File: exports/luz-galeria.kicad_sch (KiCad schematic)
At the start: 40 parts

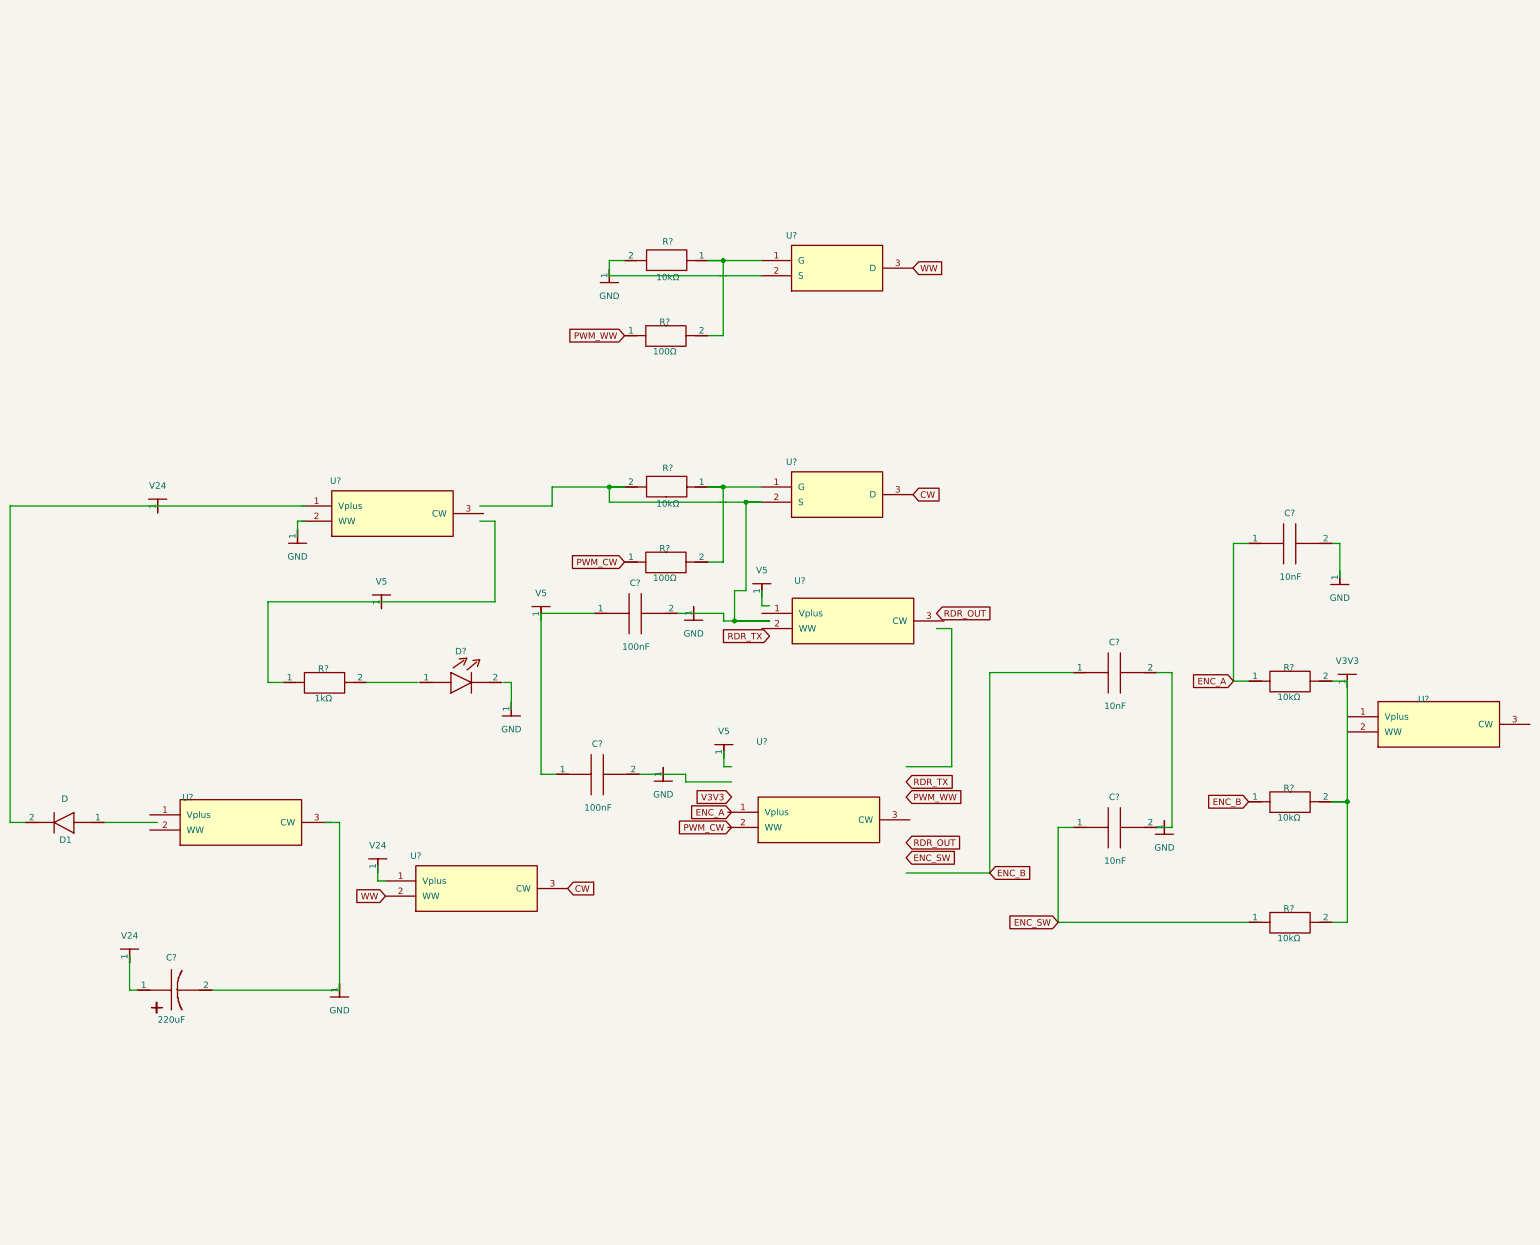
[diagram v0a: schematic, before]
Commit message: Fix EC11 encoder left unconnected by empty KiCad footprint
The kicad: footprint for the Alps EC11E resolved to zero pads in this
tscircuit version, so all seven encoder traces were silently dropped and
the encoder had no electrical connection in the netlist.

Replace it with a self-contained Ec11Footprint (geometry transcribed from
the official KiCad library: C/A/B/S1/S2 signal pads + two 2.5mm mounting
posts) with named ports, and wire MP1/MP2 to GND. Also add React keys to
the ESP32 footprint hole list to clear the render warning.

https://claude.ai/code/session_01ShC9W1aj1k3gaTpsgCGkmU
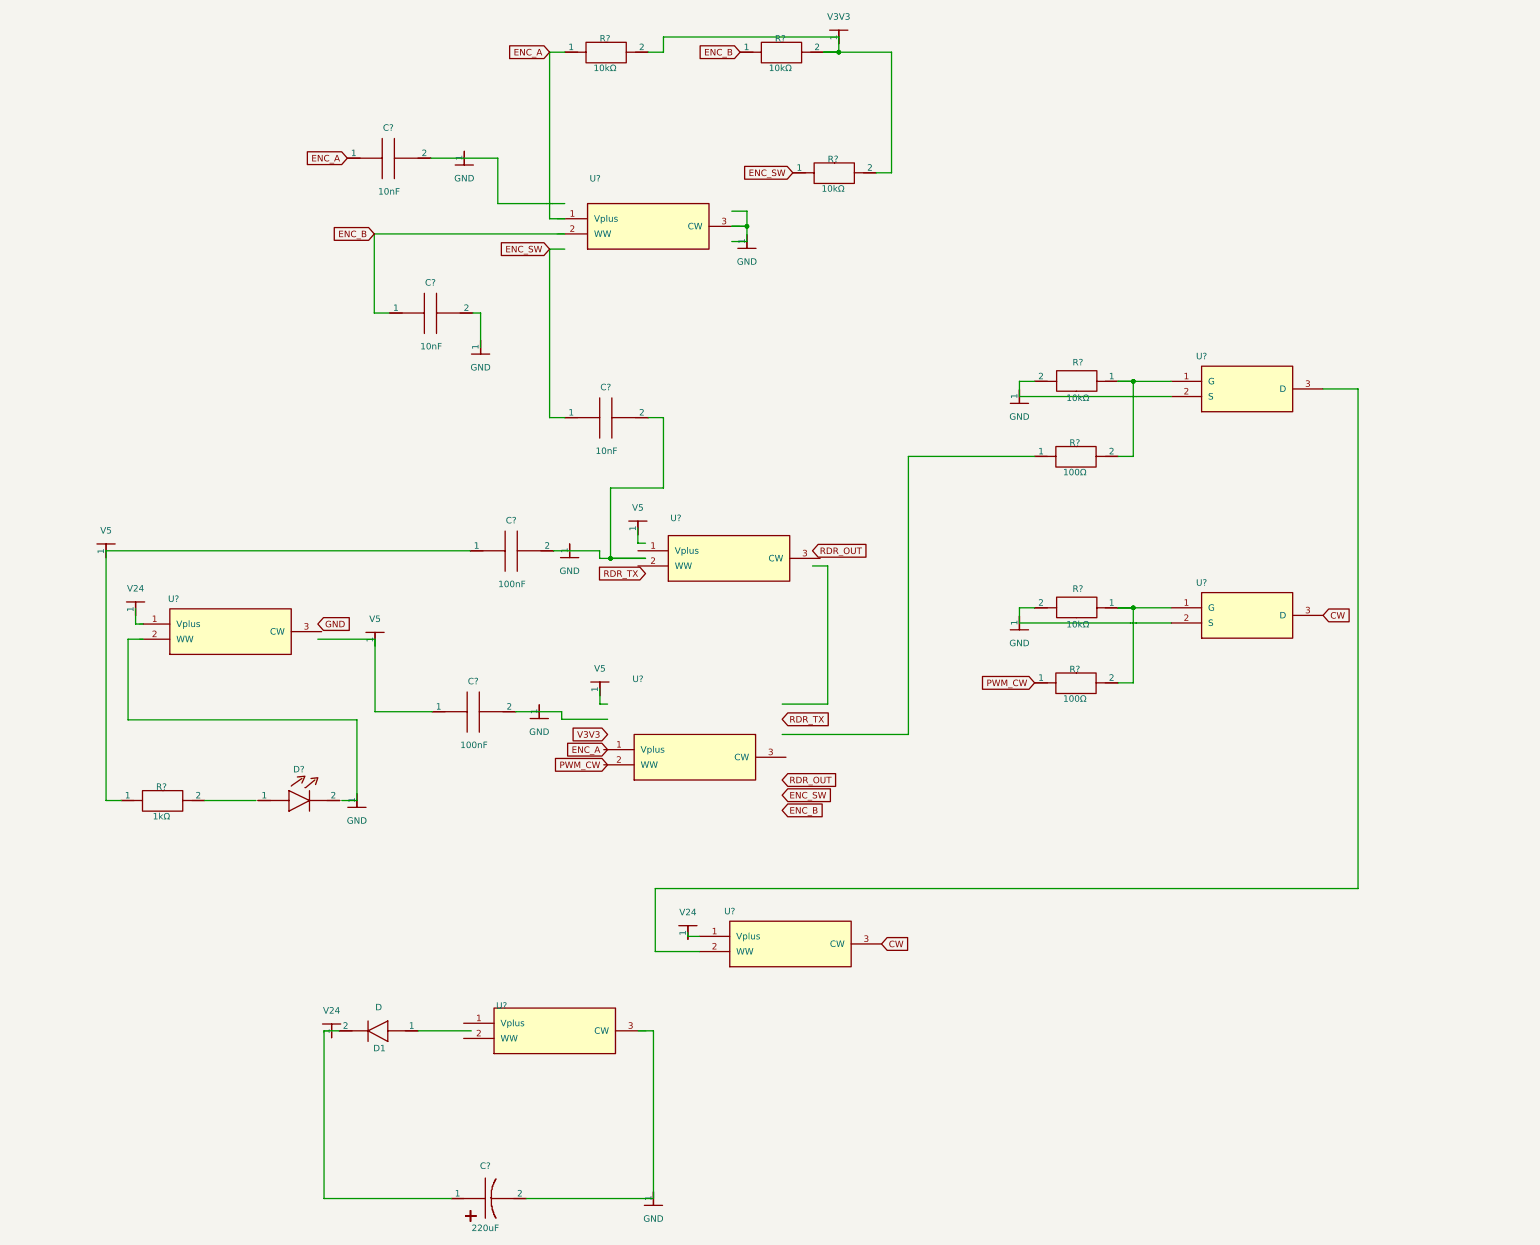
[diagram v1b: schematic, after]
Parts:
- removed C? (x2): 100nF, symbol Device:capacitor_right
- removed C? (x3): 10nF, symbol Device:capacitor_right
- removed C?: 220uF, symbol Device:capacitor_polarized_right
- removed D?: (no value), symbol Device:led_right
- removed GND (x8): GND, symbol Custom:rail_down
- removed R? (x2): 10kΩ, symbol Device:boxresistor_left
- removed R? (x2): 100Ω, symbol Device:boxresistor_right
- removed R? (x3): 10kΩ, symbol Device:boxresistor_right
- removed R?: 1kΩ, symbol Device:boxresistor_right
- removed U? (x6): (no value), symbol Device:U_chip
- removed U? (x2): (no value), symbol Device:U_chip_sot23
- removed V24 (x3): V24, symbol Custom:rail_up
- removed V5 (x4): V5, symbol Custom:rail_up
- added C? (x3): 10nF, symbol Device:capacitor_right
- added C? (x2): 100nF, symbol Device:capacitor_right
- added C?: 220uF, symbol Device:capacitor_polarized_right
- added D?: (no value), symbol Device:led_right
- added GND (x9): GND, symbol Custom:rail_down
- added R? (x3): 10kΩ, symbol Device:boxresistor_right
- added R? (x2): 10kΩ, symbol Device:boxresistor_left
- added R?: 1kΩ, symbol Device:boxresistor_right
- added R? (x2): 100Ω, symbol Device:boxresistor_right
- added U? (x2): (no value), symbol Device:U_chip_sot23
- added U? (x6): (no value), symbol Device:U_chip
- added V24 (x3): V24, symbol Custom:rail_up
- added V5 (x4): V5, symbol Custom:rail_up
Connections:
- net CW: now also U?.3 (CW), U?.3 (D)
- net ENC_A: now also C?.1
- net ENC_B: now also C?.1, R?.1
- net ENC_SW: now also C?.1, R?.1
- net PWM_CW: now also R?.1
- net at D1.2: now also C?.2 (1)
- new net: R?.2, R?.2
- new net: R?.2, U?.1 (G) (x2)
- new net: R?.2, U?.2 (S) (x2)
- new net: U?.2 (WW), U?.3 (D)
- new net: C?.2, C?.2
- new net: C?.1, R?.1

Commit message: Convert discretes to through-hole (THT) for local sourcing + hand soldering
All SMD discretes replaced with leaded parts so they can be bought in
Buenos Aires and soldered by hand (no SMD, no waiting on China):
- MOSFETs: AO3400 SOT-23 -> IRLZ44N TO-220. CRITICAL: the TO-220 pinout is
  G-D-S (pin1=Gate, pin2=Drain, pin3=Source), DIFFERENT from the SOT-23
  G-S-D. New To220Footprint has named G/D/S pads; verified in the netlist
  that Drain->strip (WW/CW) and Source->GND.
- Diode: SS34/SS54 SMA -> 1N5822 axial (AxialDiodeFootprint).
- Resistors: 0805 -> axial 1/4W (AxialResistorFootprint).
- Ceramic caps: 0805 -> leaded (CeramicCapFootprint).
- LED: 0805 -> 3mm THT (ThtLedFootprint).
Re-laid the MOSFET channels and encoder passives to fit the larger parts.
Updated docs/FABRICACION.md (BOM, soldering order, TO-220 pinout warning).

https://claude.ai/code/session_01ShC9W1aj1k3gaTpsgCGkmU
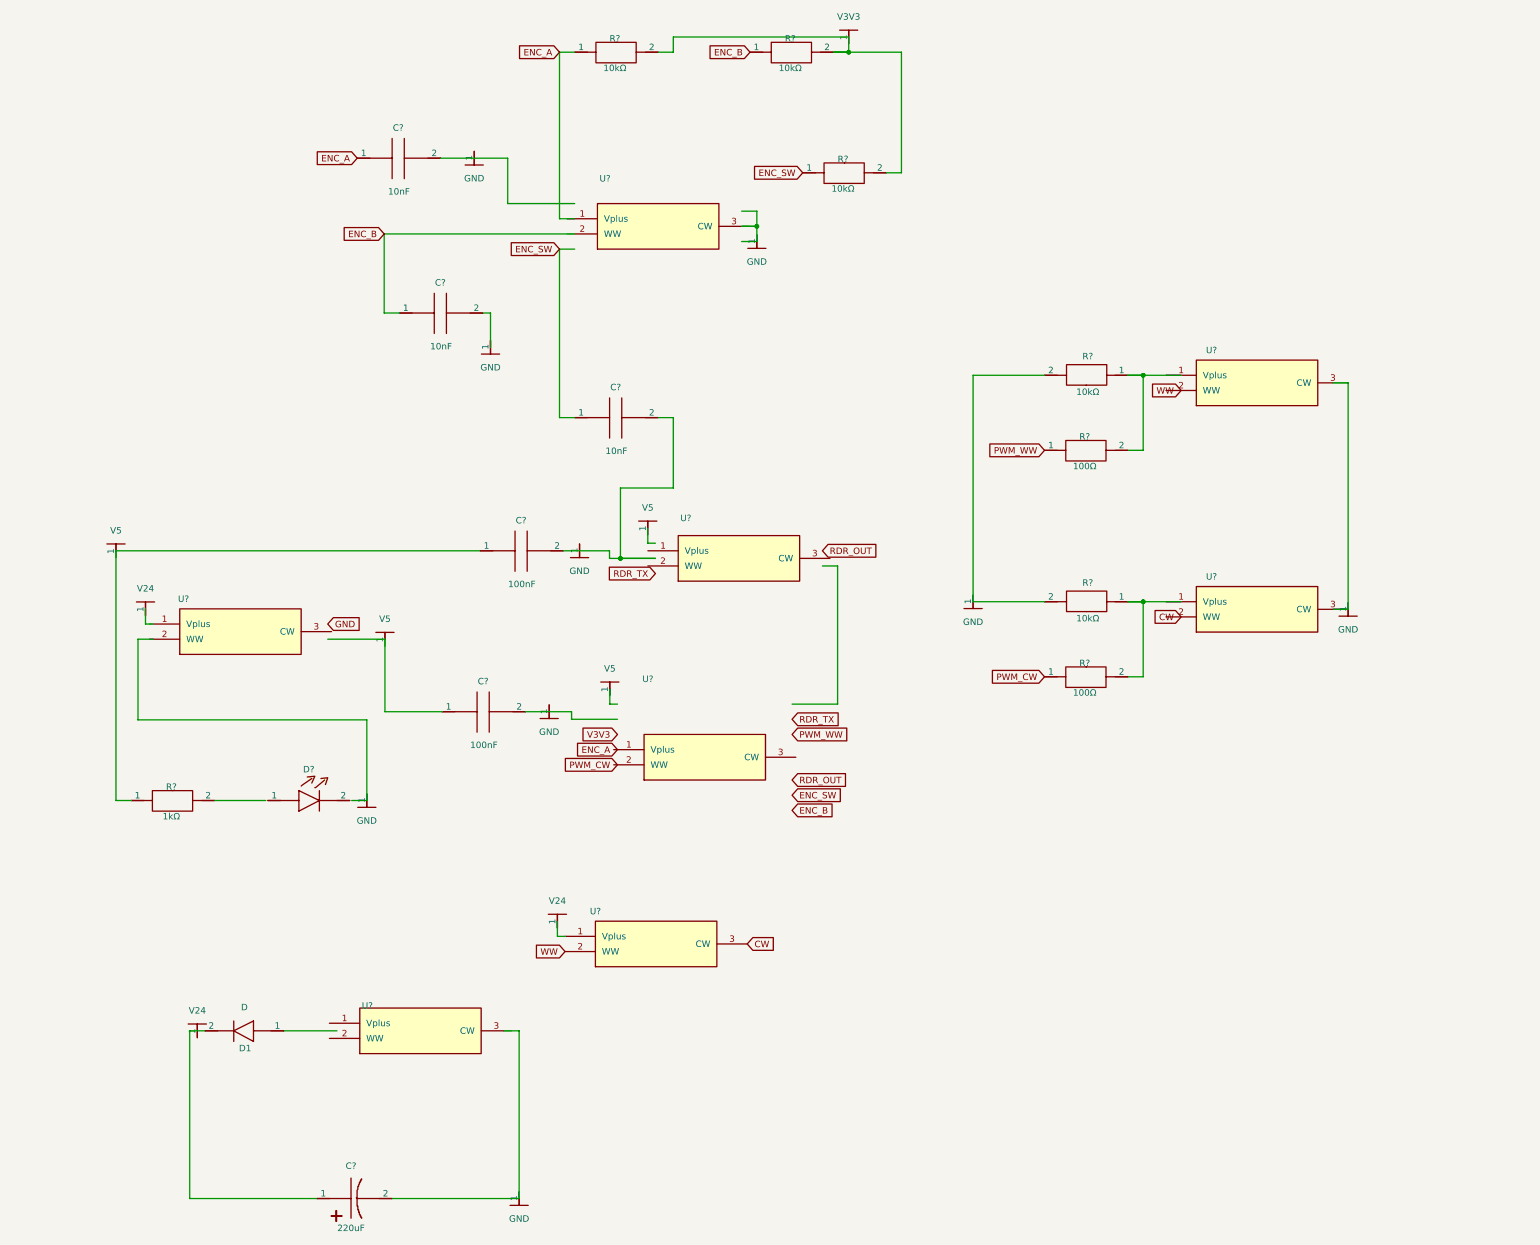
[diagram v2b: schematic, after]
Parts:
- removed C? (x3): 10nF, symbol Device:capacitor_right
- removed C? (x2): 100nF, symbol Device:capacitor_right
- removed C?: 220uF, symbol Device:capacitor_polarized_right
- removed D?: (no value), symbol Device:led_right
- removed GND (x9): GND, symbol Custom:rail_down
- removed R? (x3): 10kΩ, symbol Device:boxresistor_right
- removed R? (x2): 10kΩ, symbol Device:boxresistor_left
- removed R?: 1kΩ, symbol Device:boxresistor_right
- removed R? (x2): 100Ω, symbol Device:boxresistor_right
- removed U? (x2): (no value), symbol Device:U_chip_sot23
- removed U? (x6): (no value), symbol Device:U_chip
- removed V24 (x3): V24, symbol Custom:rail_up
- removed V5 (x4): V5, symbol Custom:rail_up
- added C?: 220uF, symbol Device:capacitor_polarized_right
- added C? (x3): 10nF, symbol Device:capacitor_right
- added C? (x2): 100nF, symbol Device:capacitor_right
- added D?: (no value), symbol Device:led_right
- added GND (x9): GND, symbol Custom:rail_down
- added R? (x2): 100Ω, symbol Device:boxresistor_right
- added R? (x2): 10kΩ, symbol Device:boxresistor_left
- added R? (x3): 10kΩ, symbol Device:boxresistor_right
- added R?: 1kΩ, symbol Device:boxresistor_right
- added U? (x8): (no value), symbol Device:U_chip
- added V24 (x3): V24, symbol Custom:rail_up
- added V5 (x4): V5, symbol Custom:rail_up
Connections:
- net CW: now also U?.3 (CW)
- net ENC_A: now also C?.1, R?.1
- net ENC_B: now also C?.1, R?.1
- net ENC_SW: now also C?.1, R?.1
- net PWM_CW: now also R?.1
- net at D1.2: now also C?.2 (1)
- new net: R?.1, R?.2 (x2)
- new net: C?.2, C?.2
- new net: C?.1, R?.1
- new net: R?.2, R?.2
- new net: R?.2, R?.2, R?.2
- new net: U?.3 (CW), U?.3 (CW)
- new net PWM_WW: R?.1
- new net WW: U?.2 (WW)
